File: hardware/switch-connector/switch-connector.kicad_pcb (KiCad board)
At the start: 2 copper layers, 38 x 28 mm, 12 parts, among them J1 Relay Control, J2 RFID connect, P1 12V, P2 Switches, P3 Pi

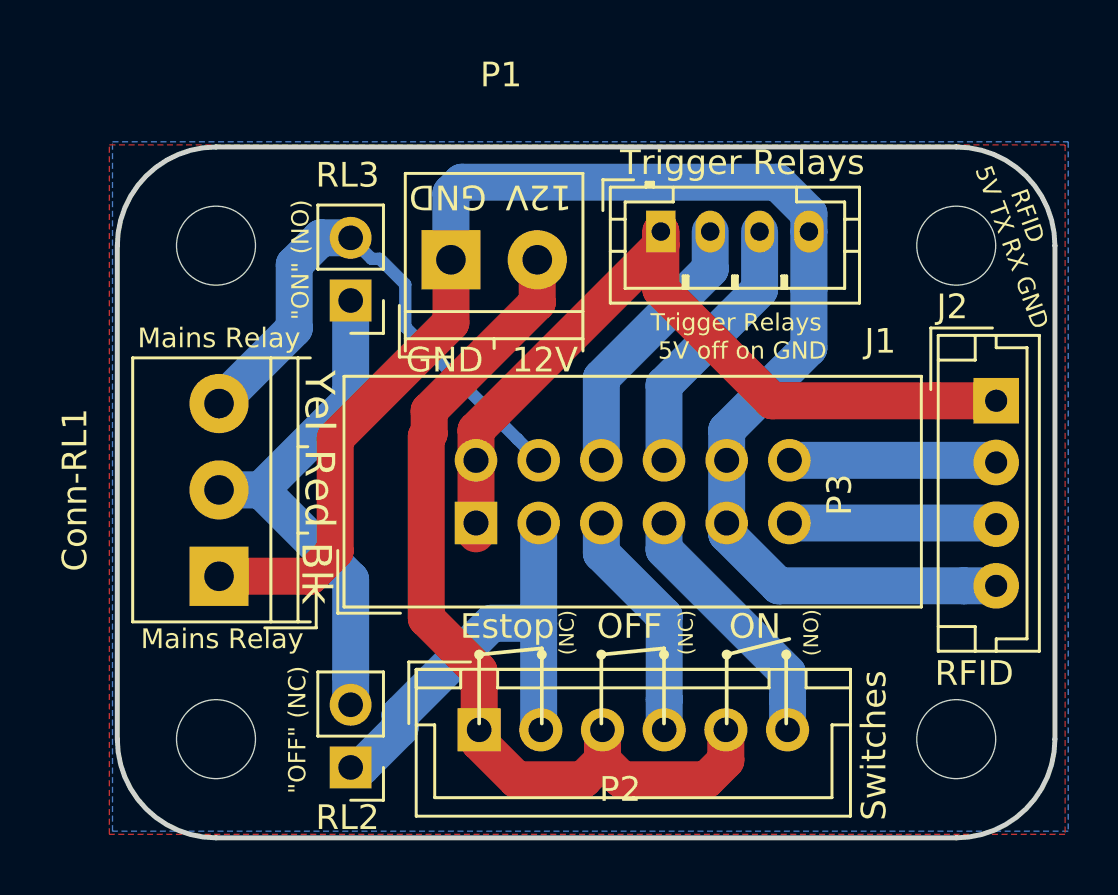
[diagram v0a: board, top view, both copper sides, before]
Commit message: Start hat for Pi to control LED panels and switch box.
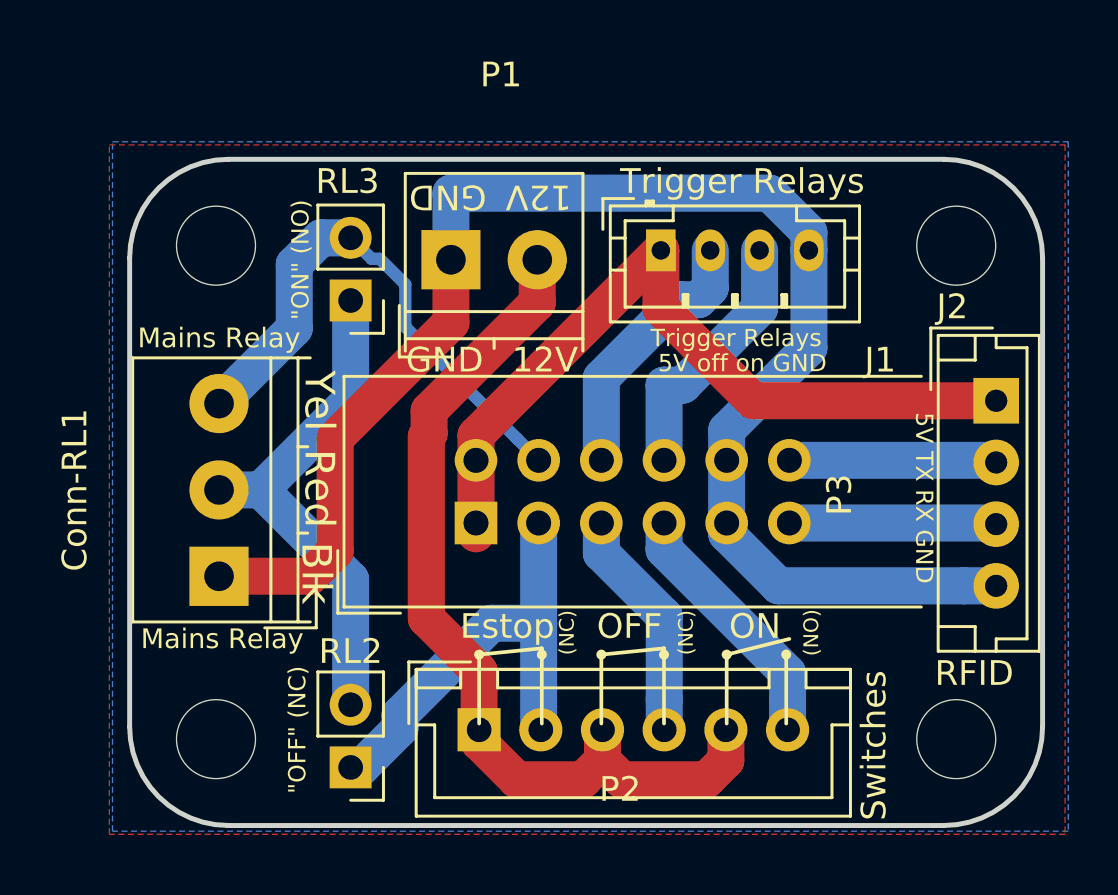
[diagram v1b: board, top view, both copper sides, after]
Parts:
- moved J1 0.76 mm to (180.0, 102.2)
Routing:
- net +5V: track 33.2 -> 32.1 mm
- net GND: track 63.0 -> 62.2 mm
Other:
- board size 38 x 28 mm -> 37 x 27 mm
